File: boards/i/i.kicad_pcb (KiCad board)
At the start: 2 copper layers, 87.3 x 170.7 mm, 9 parts, among them J17 CONN_01X02, J18 CONN_01X02, J27 CONN_01X02, U81 APA102C_x2, U84 APA102C_x5, U87 APA102C_x10, U90 APA102C_x12, U93 APA102C_x8, U96 APA102C_x3

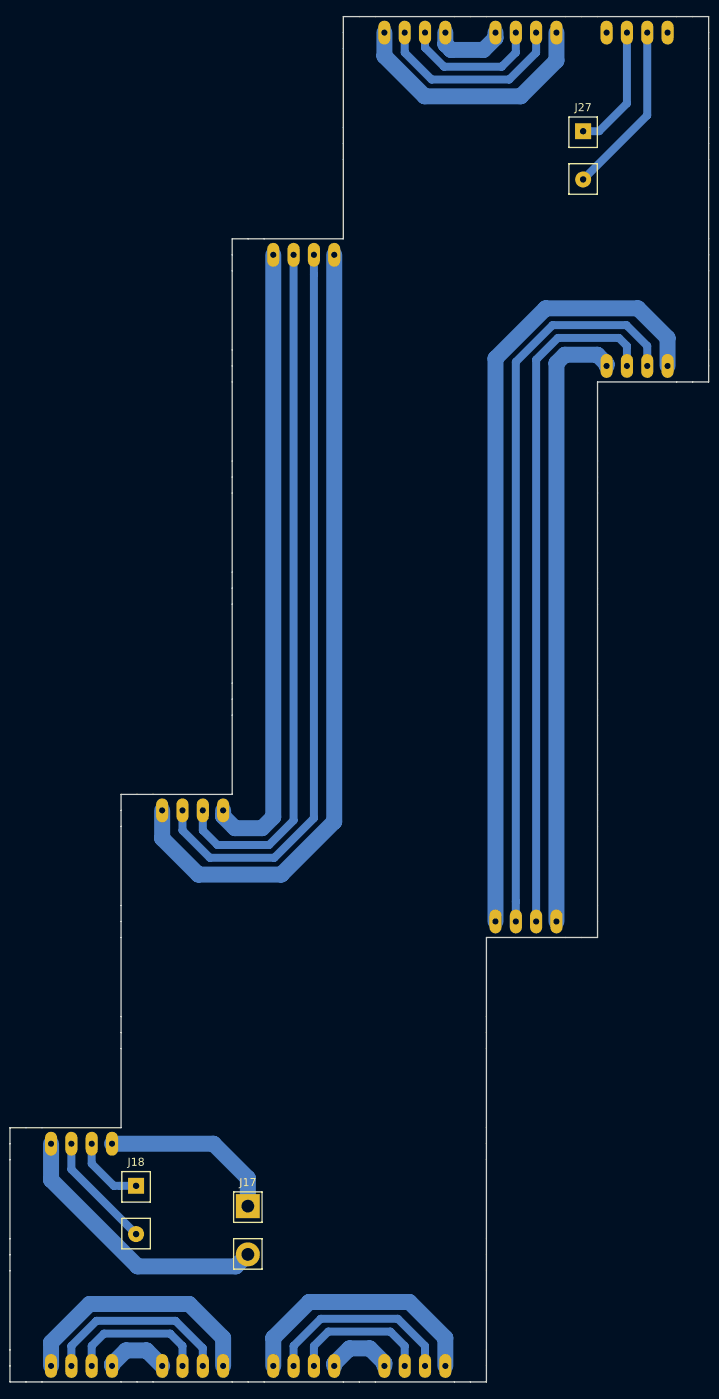
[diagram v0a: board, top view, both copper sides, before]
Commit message: Generate gerbers for all letters. Use a single drill size.
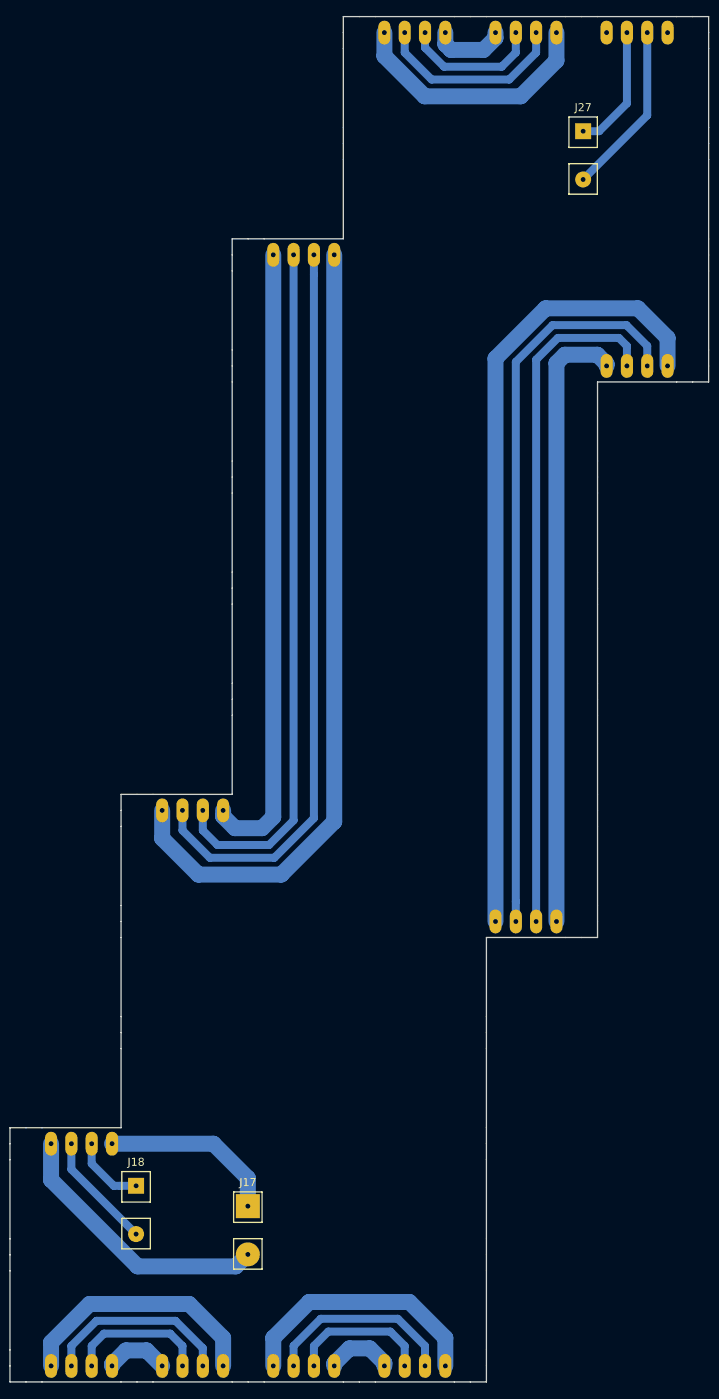
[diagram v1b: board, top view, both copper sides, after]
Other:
- net class Default: via_dia 0.6 -> None; via_drill 0.4 -> 1
- net class Signal: via_dia 0.6 -> None; via_drill 0.4 -> 1

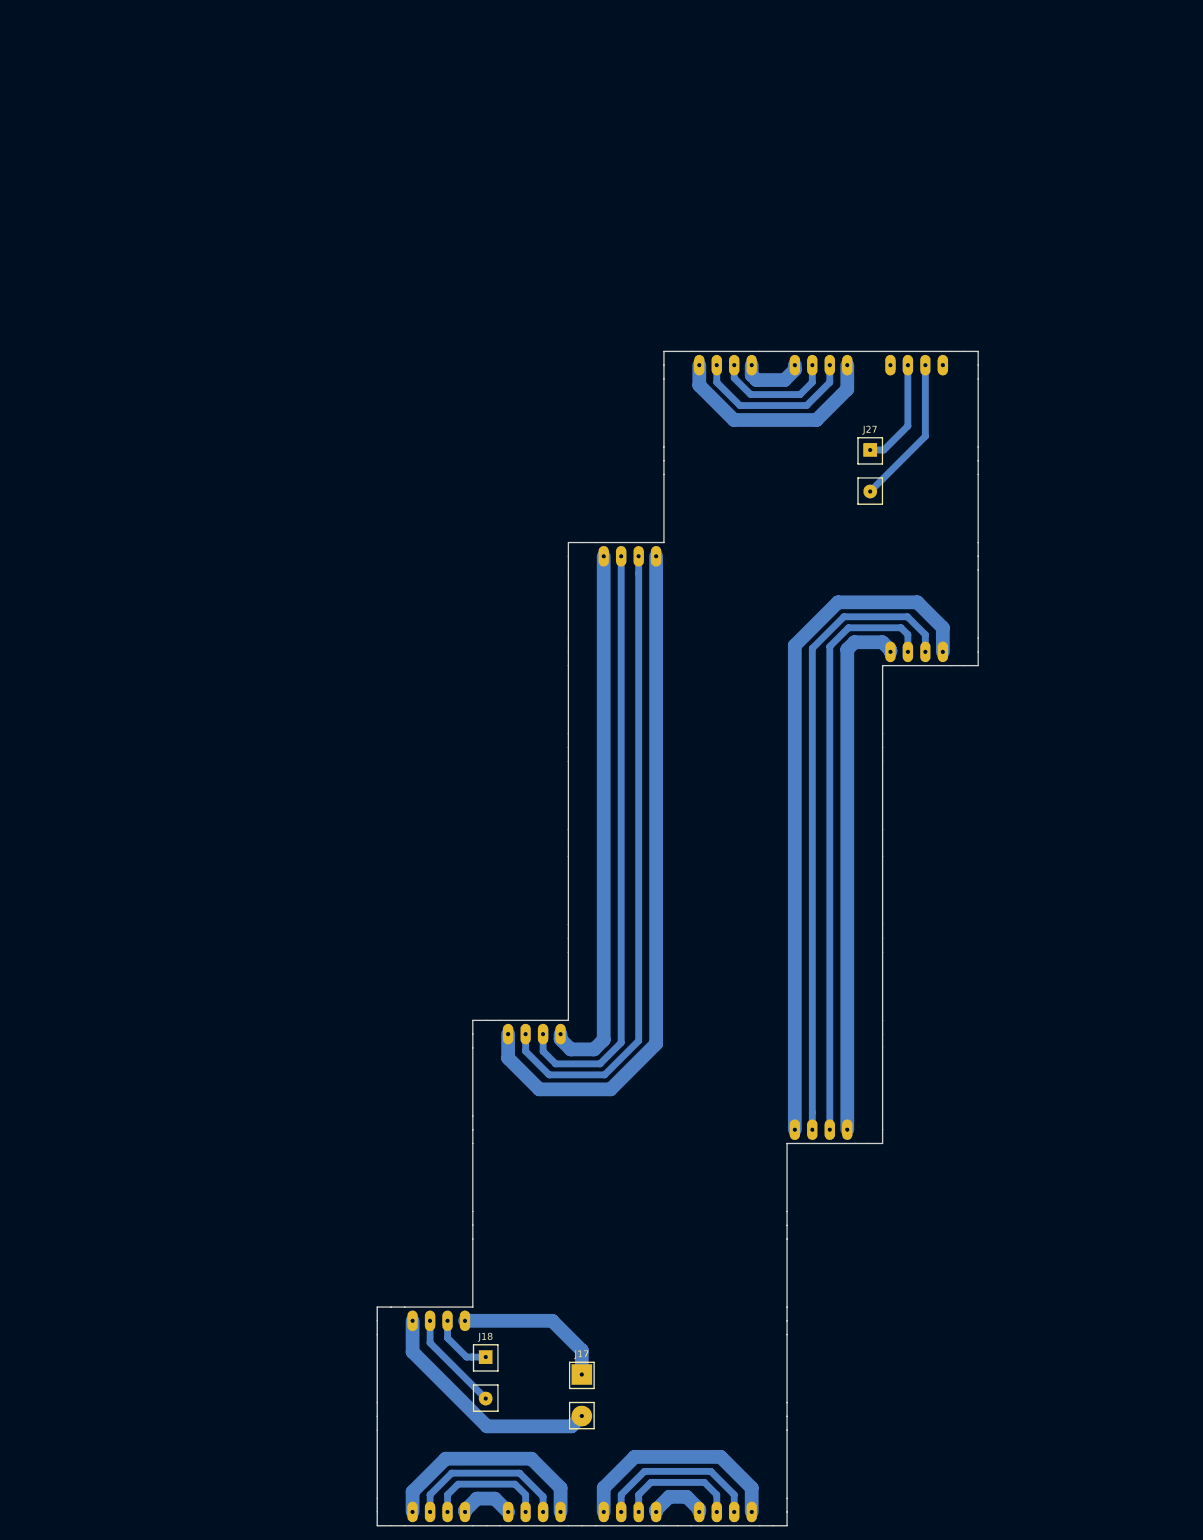
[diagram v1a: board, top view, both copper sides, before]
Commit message: Boards made! Start implementing controller.
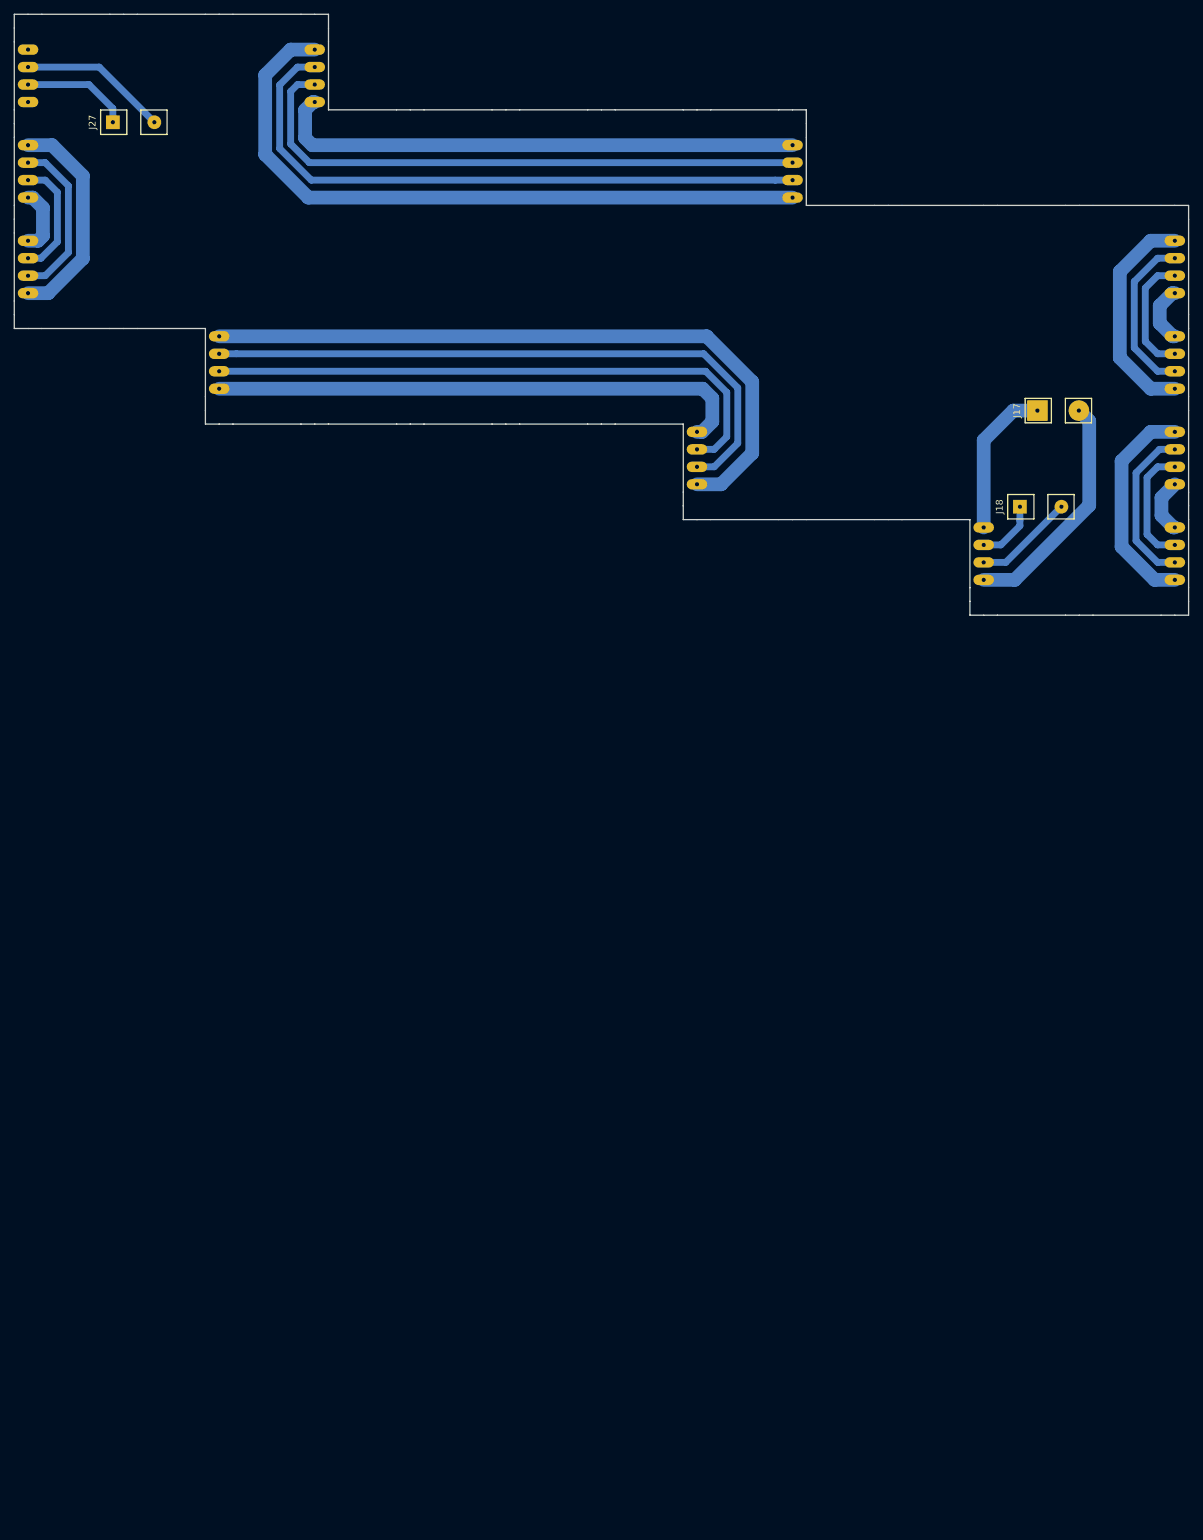
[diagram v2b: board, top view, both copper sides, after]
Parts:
- moved J17 157.7 mm to (159.2, 63.9), turned to 90 degrees
- moved U81 156.2 mm to (163.2, 84.7), turned to 0 degrees
- moved J18 148.7 mm to (156.6, 77.8), turned to 90 degrees
- moved U84 132.0 mm to (142.4, 70.8), turned to 180 degrees
- moved U96 125.2 mm to (31.3, 15.2), turned to 180 degrees
- moved J27 118.9 mm to (24.8, 22.0), turned to 90 degrees
- moved U93 102.8 mm to (66.0, 29.1), turned to 0 degrees
- moved U90 99.3 mm to (93.8, 43.0), turned to 180 degrees
- moved U87 98.1 mm to (107.7, 56.9), turned to 0 degrees
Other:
- board size 87.3 x 170.7 mm -> 170.7 x 87.3 mm
- net class Default: via_dia None -> 0.6; via_drill 1 -> 0.6
- net class Signal: via_dia None -> 0.6; via_drill 1 -> 0.6
